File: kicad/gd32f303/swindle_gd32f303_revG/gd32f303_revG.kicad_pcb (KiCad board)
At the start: 2 copper layers, 49.2 x 31.7 mm, 57 parts, among them J1 Debug port, J2 Debug port, J3 USB, J4 DFU, J5 BOOT, J6 jtag, J9 Conn_01x03_Socket, U1 GD32F303, U2 3V->VTREF, U3 VTREF->3V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

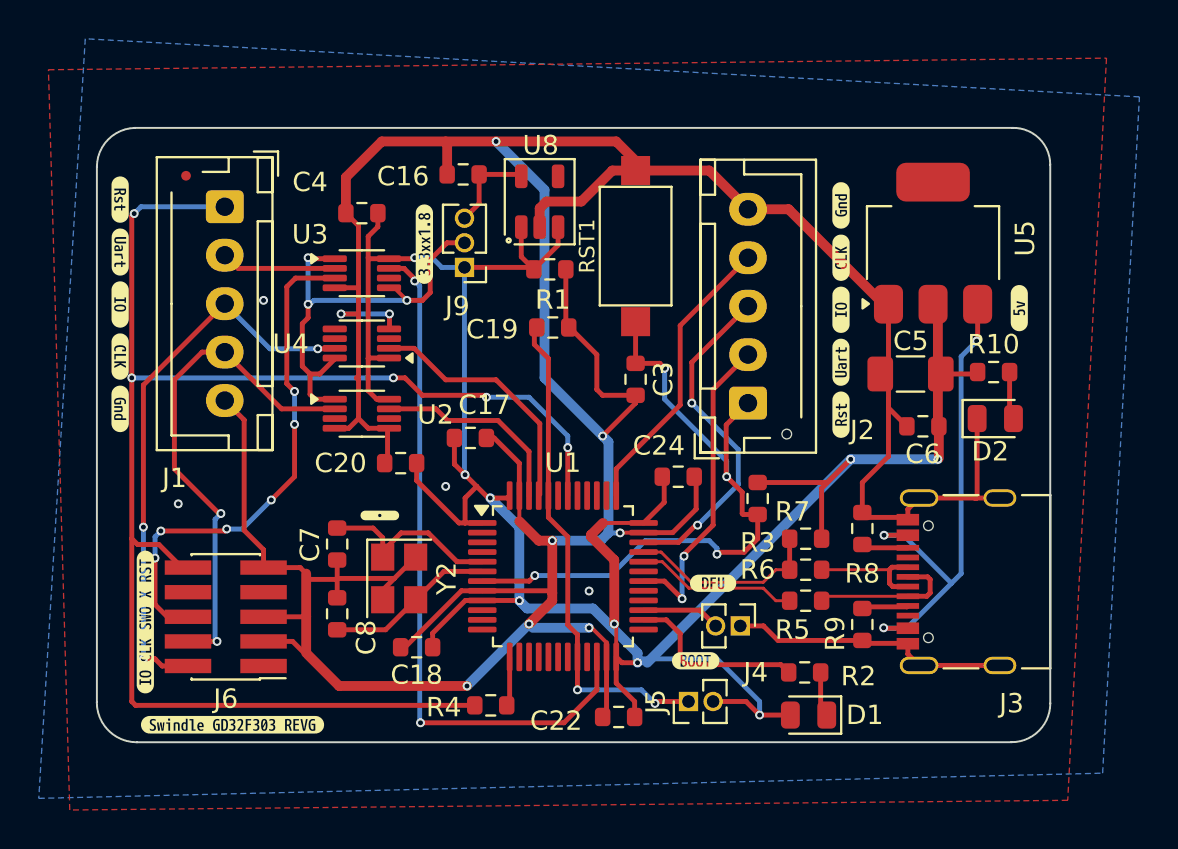
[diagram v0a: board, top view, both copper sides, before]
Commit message: update usb C connector + add 3 free pins
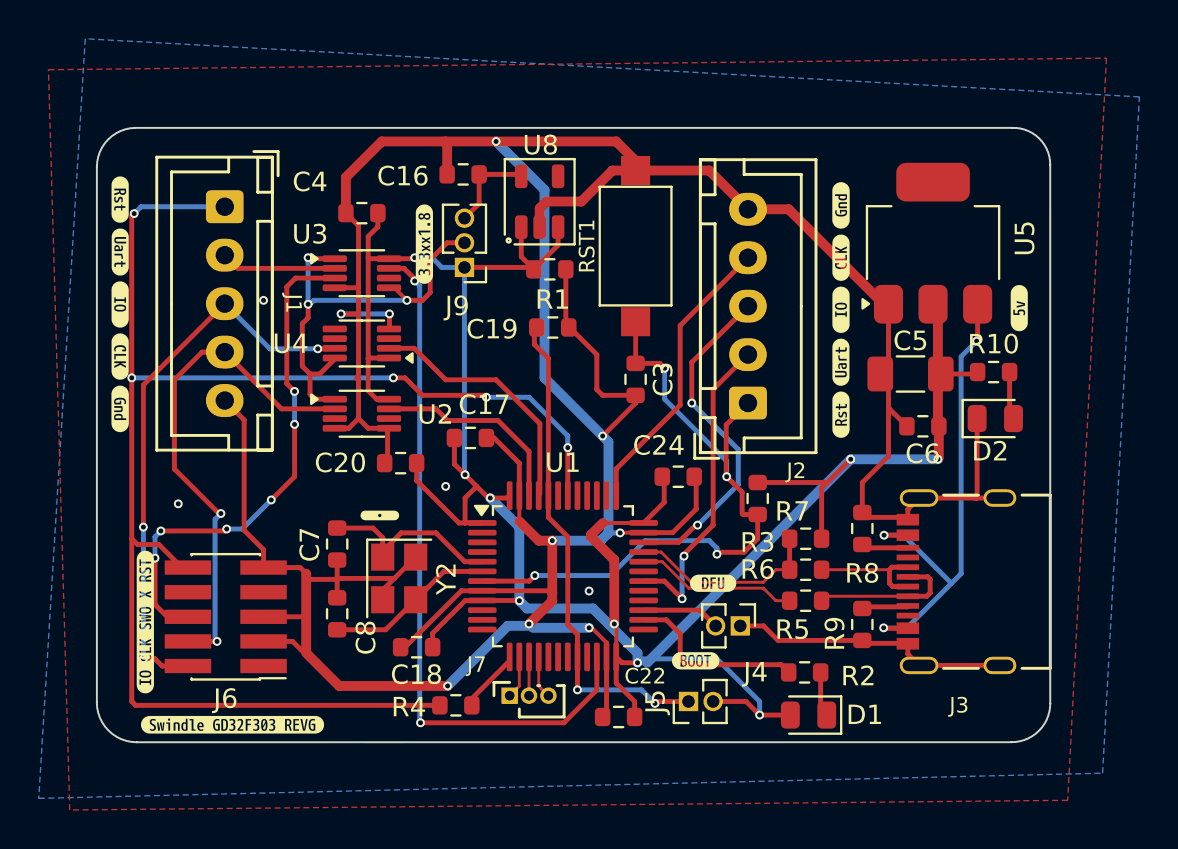
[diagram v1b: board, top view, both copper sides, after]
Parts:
- added J7: Conn_01x03_Pin, Connector_PinSocket_1.00mm:PinSocket_1x03_P1.00mm_Vertical, F.Cu at (127.5, 97.6)
- J1, J2: footprint Connector_JST:JST_XH_B5B-XH-AM_1x05_P2.50mm_Vertical -> Connector_JST:JST_XH_B5B-XH-A_1x05_P2.50mm_Vertical
- J3: footprint Connector_USB:USB_C_Receptacle_Palconn_UTC16-G -> Library:USB_C_Receptacle_Palconn_UTC16-G_no_hole
- moved R4 1.80 mm to (124.7, 98.1)
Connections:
- U1 pad 14: unconnected-(U1-PA4-Pad14) -> Net-(J7-Pin_1)
- U1 pad 15: unconnected-(U1-PA5-Pad15) -> Net-(J7-Pin_2)
- U1 pad 16: unconnected-(U1-PA6-Pad16) -> Net-(J7-Pin_3)
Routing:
- net Net-(J7-Pin_3): track 0.00 -> 2.21 mm
- net Net-(J7-Pin_1): track 0.00 -> 2.21 mm
- net Net-(J7-Pin_2): track 0.00 -> 2.00 mm
- net INOUT_NRESET: track 77.9 -> 76.1 mm

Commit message: kicad: update GD32 PCB with SWDIO_DIR
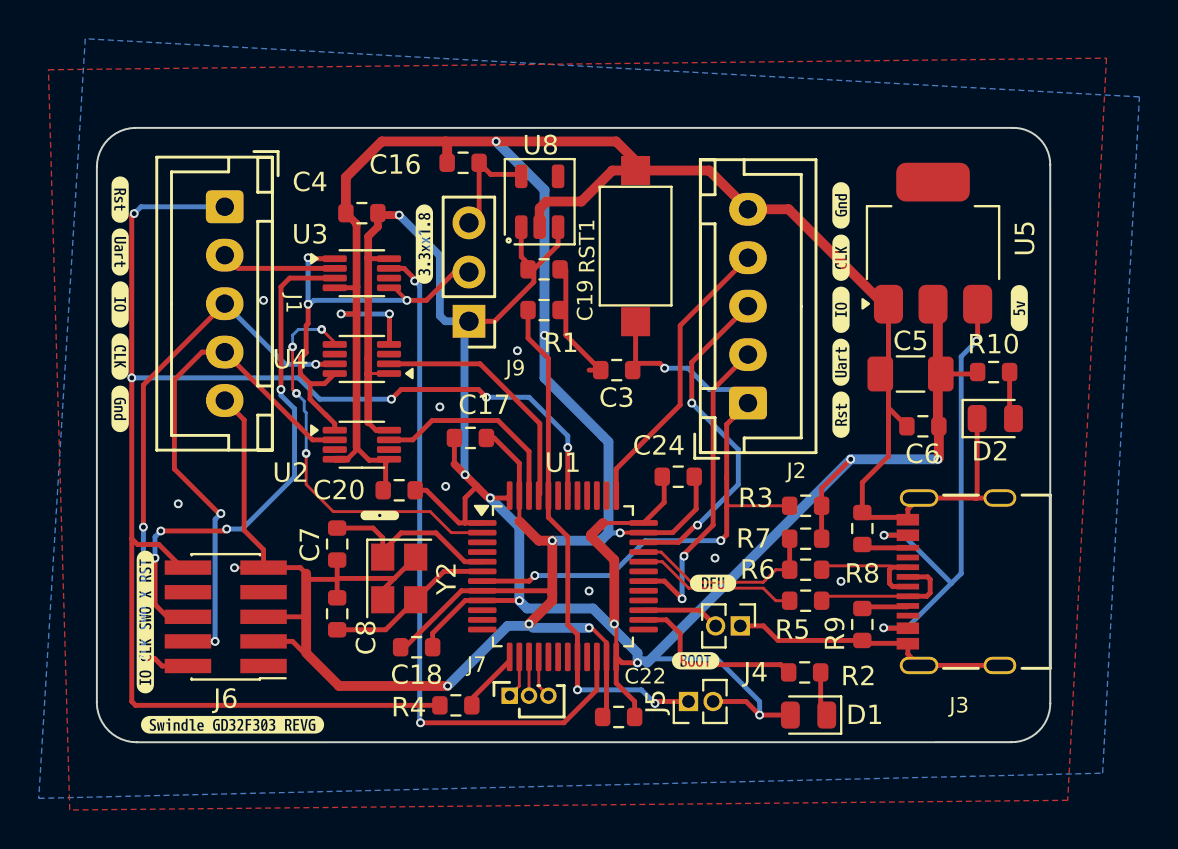
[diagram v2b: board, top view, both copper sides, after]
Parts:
- J9: footprint Connector_PinHeader_1.27mm:PinHeader_1x03_P1.27mm_Vertical -> Connector_PinHeader_2.54mm:PinHeader_1x03_P2.54mm_Vertical
- moved J9 2.79 mm to (125.4, 78.3)
- moved R3 2.50 mm to (142.8, 87.8), turned to 180 degrees
- moved U2 1.60 mm to (119.9, 84.7)
- moved C20 1.40 mm to (121.8, 87.0)
- moved C3 1.08 mm to (133.0, 80.8), turned to 180 degrees
- moved R1 1.01 mm to (129.3, 77.7)
- moved U4 0.80 mm to (119.9, 80.2)
- moved C16 0.60 mm to (125.1, 70.1)
- moved C19 0.30 mm to (129.3, 75.6)
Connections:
- U1 pad 2: unconnected-(U1-PC13-Pad2) -> SWIO_DIR_3V
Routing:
- net SWIO_DIR_3V: track 0.00 -> 20.8 mm, vias 0 -> 4
- net NRST: track 35.1 -> 33.0 mm, vias 4 -> 3
- net +3.3V: track 136.9 -> 135.6 mm
- net Net-(J5-Pin_1): track 25.5 -> 26.7 mm
- net GND: track 217.8 -> 216.7 mm, vias 13 -> 18
- net V1.8: track 4.65 -> 5.65 mm
- net OUT_SWDCLK: track 26.1 -> 26.8 mm
- net INOUT_SWO: track 25.5 -> 25.9 mm, vias 6 -> 4

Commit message: kicad: GD32, change the DIR pin to PA1
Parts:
- moved D1 0.40 mm to (142.5, 98.7)
- moved R2 0.27 mm to (142.5, 96.3)
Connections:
- U1 pad 11: unconnected-(U1-PA1-Pad11) -> SWIO_DIR_3V
- U1 pad 2: SWIO_DIR_3V -> unconnected-(U1-PC13-Pad2)
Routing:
- net SWIO_DIR_3V: track 20.8 -> 26.1 mm, vias 4 -> 6
- net +3.3V: track 135.6 -> 134.5 mm

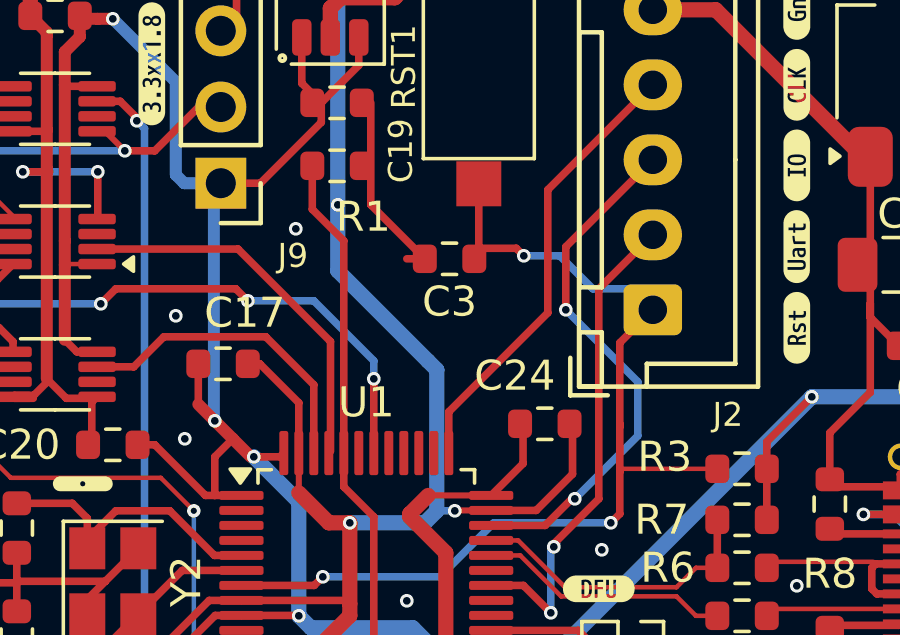
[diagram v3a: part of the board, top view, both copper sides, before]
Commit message: kicad: GD32, change the DIR pin to PA1
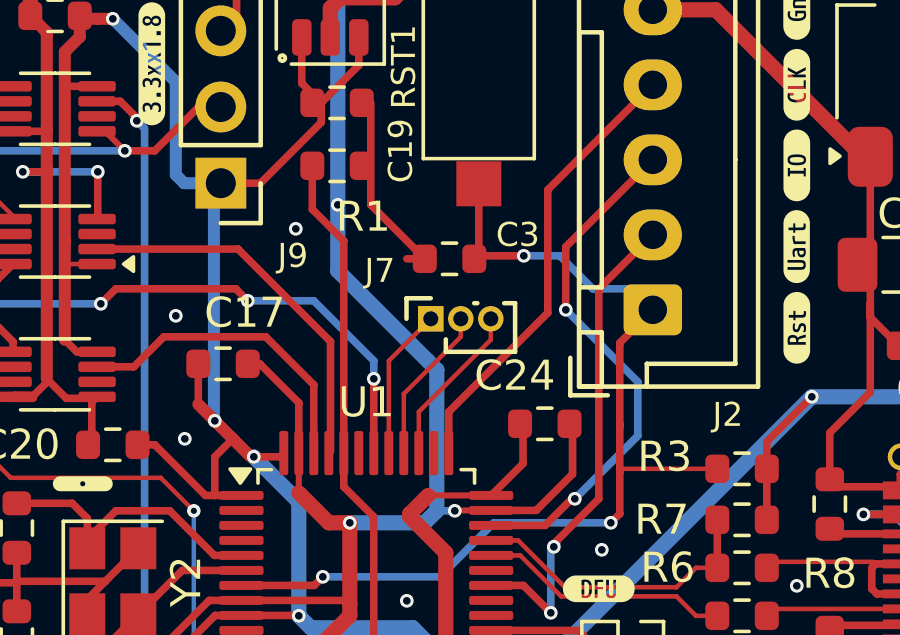
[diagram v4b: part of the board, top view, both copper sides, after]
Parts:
- added J7: Conn_01x03_Pin, Connector_PinSocket_1.00mm:PinSocket_1x03_P1.00mm_Vertical, F.Cu at (132.4, 82.8)
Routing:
- net unconnected-(U1-PB3-Pad39): track 0.00 -> 5.47 mm
- net unconnected-(U1-PB4-Pad40): track 0.00 -> 5.26 mm
- net unconnected-(U1-PB5-Pad41): track 0.00 -> 5.05 mm

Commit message: update GD32 pcb
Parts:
- removed the J7 at (132.4, 82.8)
- added J8: ~, Connector_PinSocket_1.27mm:PinSocket_1x05_P1.27mm_Vertical, F.Cu at (125.9, 98.2)
- J2: footprint Connector_JST:JST_XH_B5B-XH-A_1x05_P2.50mm_Vertical -> Connector_PinSocket_1.27mm:PinSocket_1x05_P1.27mm_Vertical
- J7: value Conn_01x03_Pin -> Conn_01x05_Pin; footprint Connector_PinSocket_1.00mm:PinSocket_1x03_P1.00mm_Vertical -> Connector_PinSocket_1.27mm:PinSocket_1x05_P1.27mm_Vertical
- moved J7 17.4 mm to (134.5, 81.7), turned to 180 degrees
- moved RST1 6.77 mm to (140.7, 73.4)
- moved C3 5.22 mm to (137.7, 78.5), turned to -90 degrees
- moved J2 2.29 mm to (140.7, 84.6), turned to 180 degrees
- moved R4 2.00 mm to (122.7, 98.1)
- moved C22 0.49 mm to (133.6, 98.8)
- moved U1 0.47 mm to (130.2, 91.0)
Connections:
- J7 pad 1: Net-(J7-Pin_1) -> PB3
- J7 pad 2: Net-(J7-Pin_2) -> PB4
- J7 pad 3: Net-(J7-Pin_3) -> PB5
- U1 pad 14: Net-(J7-Pin_1) -> PA4
- U1 pad 15: Net-(J7-Pin_2) -> PA5
- U1 pad 16: Net-(J7-Pin_3) -> PA6
- U1 pad 17: unconnected-(U1-PA7-Pad17) -> PA7
- U1 pad 18: unconnected-(U1-PB0-Pad18) -> PB0
- U1 pad 39: unconnected-(U1-PB3-Pad39) -> PB3
- U1 pad 40: unconnected-(U1-PB4-Pad40) -> PB4
- U1 pad 41: unconnected-(U1-PB5-Pad41) -> PB5
- U1 pad 43: unconnected-(U1-PB7-Pad43) -> PB7
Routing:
- net GND: track 216.7 -> 236.5 mm, vias 18 -> 20
- net PB7: track 0.00 -> 11.2 mm
- net PB5: track 0.00 -> 9.56 mm
- net PB4: track 0.00 -> 8.19 mm
- net PB3: track 0.00 -> 6.61 mm
- net SWDIO: track 17.5 -> 11.8 mm
- net unconnected-(U1-PB3-Pad39): track 5.47 -> 0.00 mm
- net unconnected-(U1-PB4-Pad40): track 5.26 -> 0.00 mm
- net unconnected-(U1-PB5-Pad41): track 5.05 -> 0.00 mm
- net PA4: track 0.00 -> 3.98 mm
- net SWDCLK: track 15.1 -> 11.3 mm
- net PB0: track 0.00 -> 3.46 mm
- net PA5: track 0.00 -> 3.37 mm
- net PA7: track 0.00 -> 3.11 mm
- net PA6: track 0.00 -> 3.05 mm
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
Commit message: kicad : update gd32
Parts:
- moved C4 1.25 mm to (119.9, 71.5)
- moved U3 1.25 mm to (119.8, 74.5)
- moved U4 0.72 mm to (119.9, 79.5)
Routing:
- net +3.3V: track 135.2 -> 137.2 mm
- net INOUT_SWO: track 25.9 -> 27.2 mm
- net OUT_UART_RX_3V: track 38.0 -> 39.1 mm
- net GND: track 236.5 -> 235.8 mm
- net Net-(U1-PB13): track 9.86 -> 9.29 mm
- net SWIO_DIR_3V: track 26.7 -> 27.2 mm
- net VTREF: track 22.6 -> 23.1 mm

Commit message: update gd32 pcb to revG
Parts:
- removed kibuzzard-672326BE: G***, kibuzzard-672326BE
- added kibuzzard-683DE1D5: G***, kibuzzard-683DE1D5, F.Cu at (113.2, 99.1)
- added kibuzzard-683DFE0C: G***, kibuzzard-683DFE0C, F.Cu at (144.7, 98.7)
- added kibuzzard-683DFE0C: G***, kibuzzard-683DFE0C, F.Cu at (151.1, 84.8)
- U2, U3, U4: footprint Package_SO:VSSOP-8_2.3x2mm_P0.5mm -> Package_SO:TSSOP-8_3x3mm_P0.65mm
- moved RST1 2.53 mm to (138.5, 72.2), turned to 180 degrees
- moved U3 0.25 mm to (119.6, 74.5)
- moved C20 0.25 mm to (121.8, 87.2)
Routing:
- net NRST: track 35.2 -> 41.4 mm
- net GND: track 235.8 -> 240.8 mm
- net OUT_SWDIO: track 28.1 -> 30.4 mm
- net VTREF: track 23.1 -> 21.7 mm
- net INOUT_SWO: track 27.2 -> 26.1 mm
- net OUT_UART_RX_3V: track 39.1 -> 40.1 mm
- net OUT_UART_RX: track 6.13 -> 5.51 mm, vias 0 -> 1
- net OUT_SWDCLK: track 26.8 -> 26.5 mm, vias 2 -> 3
- net OUT_SWDCLK_3V: track 10.6 -> 10.4 mm, vias 0 -> 1
- net OUT_SWDIO_3V: track 13.4 -> 13.3 mm, vias 0 -> 1
